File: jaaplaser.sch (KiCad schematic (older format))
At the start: 11 parts

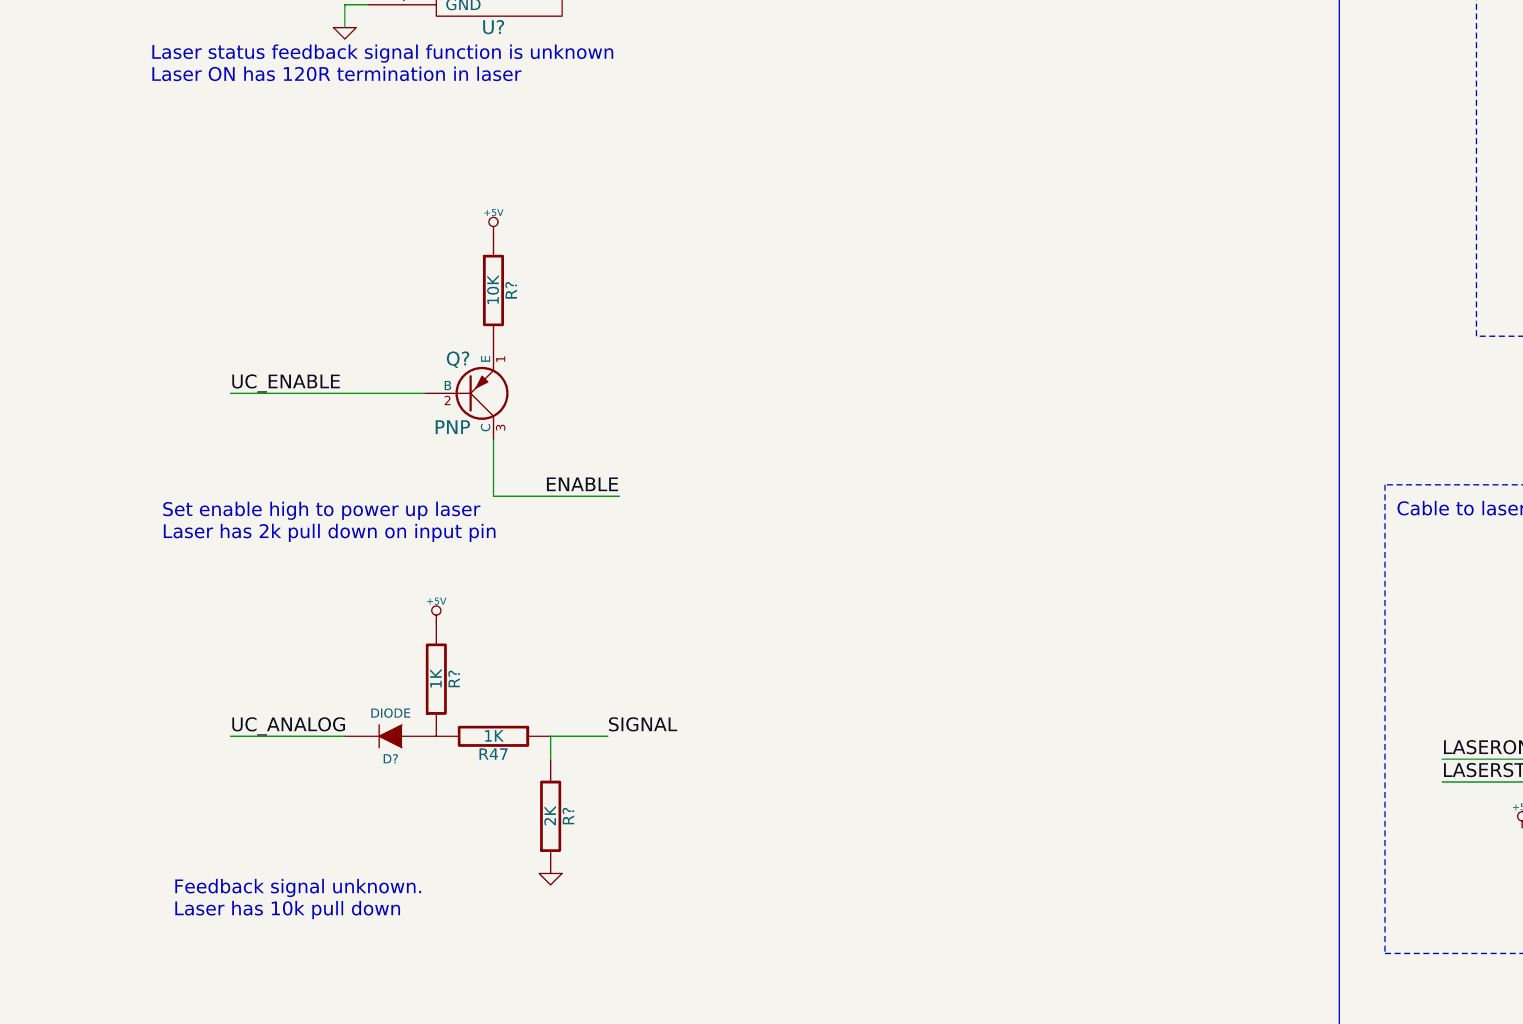
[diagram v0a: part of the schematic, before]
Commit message: added opto-coupler and connections
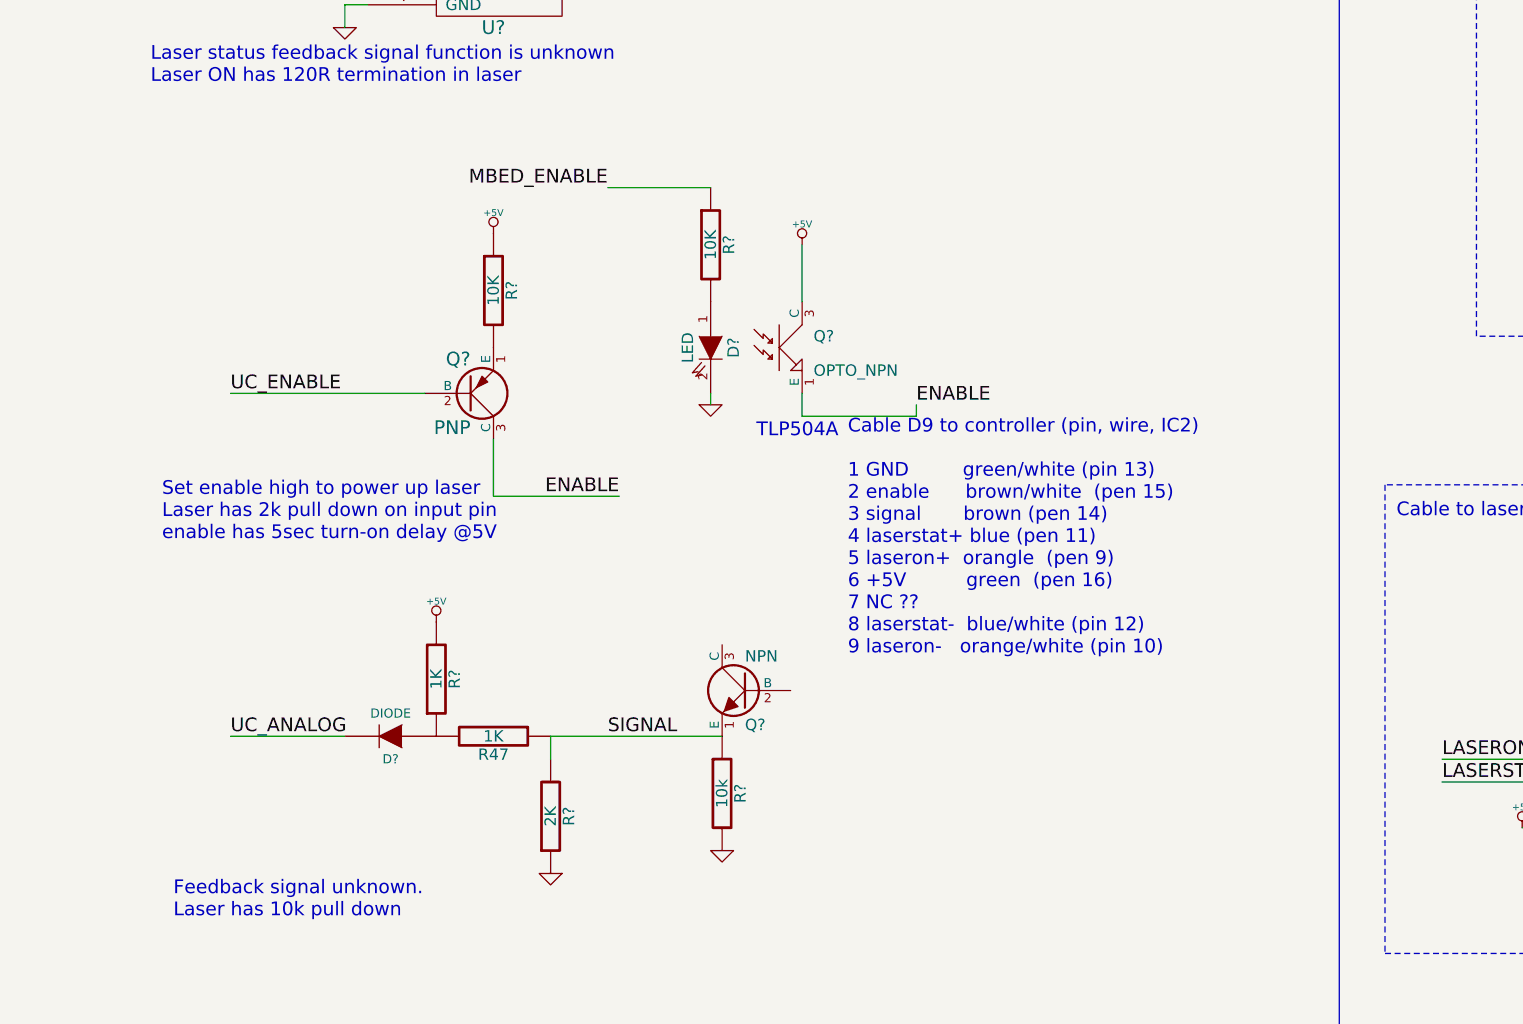
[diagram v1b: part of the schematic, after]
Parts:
- added D?: LED, symbol LED
- added Q?: NPN, symbol NPN
- added Q?: OPTO_NPN, symbol OPTO_NPN
- added R?: 10k, symbol R
- added R?: 10K, symbol R
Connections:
- net +5V: now also Q?.3 (C)
- net ENABLE: now also Q?.1 (E)
- net GND: now also D?.2 (K), R?.2
- net SIGNAL: now also Q?.1 (E), R?.1
- new net: D?.1 (A), R?.2
- new net MBED_ENABLE: R?.1
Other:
- note added: "Cable D9 to controller (pin, wire, IC2)\n\n1 GND green/white (pin 13)\n2 enable brown/white (pen 15)\n3 signal brown (pen 14)\n4 laserstat+ blue (pen 11)\n5 laseron+ orangle (pen 9)\n6 +5V green (pen 16)\n7 NC ?? \n8 laserstat- blue/white (pin 12)\n9 laseron- orange/white (pin 10)\n"
- note added: "Set enable high to power up laser\nLaser has 2k pull down on input pin\nenable has 5sec turn-on delay @5V\n"
- note added: "TLP504A"
- note removed: "Set enable high to power up laser\nLaser has 2k pull down on input pin"
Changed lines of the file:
@@
-EESchema Schematic File Version 2  date 6/1/2014 23:12:49
+EESchema Schematic File Version 2  date 11/22/2015 18:08:19
 LIBS:power
 LIBS:device
@@
 Sheet 1 1
 Title "Lumunics Efx Laser interface"
-Date "1 jun 2014"
+Date "22 nov 2015"
 Rev "1"
 Comp "LaosLaser.org"
@@
 Comment4 ""
 $EndDescr
-Text Notes 7000 4750 0    60   ~ 0
-Cable to laser Header to DB9-Female (flat cable)
+Text Notes 4200 4400 0    60   ~ 0
+TLP504A
+Text Label 3550 3300 2    60   ~ 0
+MBED_ENABLE
+Wire Wire Line
+	4000 3300 3550 3300
+Wire Wire Line
+	4000 4200 4000 4250
+Wire Wire Line
+	4050 5700 3300 5700
 Wire Notes Line
 	11100 4600 11100 6650
@@
 Wire Wire Line
 	3050 4650 3050 4400
-Wire Wire Line
-	3550 5700 3300 5700
 Connection ~ 4500 2300
 Wire Wire Line
@@
 Wire Wire Line
 	9600 5300 9600 5350
+Wire Wire Line
+	4400 3550 4400 3800
+Wire Wire Line
+	4400 4200 4400 4300
+Wire Wire Line
+	4400 4300 4900 4300
+Wire Wire Line
+	4900 4300 4900 4250
+$Comp
+L R R?
+U 1 1 5651F627
+P 4000 3550
+F 0 "R?" V 4080 3550 50  0000 C CNN
+F 1 "10K" V 4000 3550 50  0000 C CNN
+	1    4000 3550
+	1    0    0    -1
+$EndComp
+Text Label 4900 4250 0    60   ~ 0
+ENABLE
+$Comp
+L GND #PWR?
+U 1 1 5651F603
+P 4000 4250
+F 0 "#PWR?" H 4000 4250 30  0001 C CNN
+F 1 "GND" H 4000 4180 30  0001 C CNN
+	1    4000 4250
+	1    0    0    -1
+$EndComp
+$Comp
+L +5V #PWR?
+U 1 1 5651F5F5
+P 4400 3550
+F 0 "#PWR?" H 4400 3640 20  0001 C CNN
+F 1 "+5V" H 4400 3640 30  0000 C CNN
+	1    4400 3550
+	1    0    0    -1
+$EndComp
+$Comp
+L LED D?
+U 1 1 5651F5E6
+P 4000 4000
+F 0 "D?" H 4000 4100 50  0000 C CNN
+F 1 "LED" H 4000 3900 50  0000 C CNN
+	1    4000 4000
+	0    1    1    0
+$EndComp
+$Comp
+L OPTO_NPN Q?
+U 1 1 5651F5D6
+P 4300 4000
+F 0 "Q?" H 4450 4050 50  0000 L CNN
+F 1 "OPTO_NPN" H 4450 3900 50  0000 L CNN
+	1    4300 4000
+	1    0    0    -1
+$EndComp
+$Comp
+L GND #PWR?
+U 1 1 5651CAA0
+P 4050 6200
+F 0 "#PWR?" H 4050 6200 30  0001 C CNN
+F 1 "GND" H 4050 6130 30  0001 C CNN
+	1    4050 6200
+	-1   0    0    -1
+$EndComp
+$Comp
+L R R?
+U 1 1 5651CA94
+P 4050 5950
+F 0 "R?" V 4130 5950 50  0000 C CNN
+F 1 "10k" V 4050 5950 50  0000 C CNN
+	1    4050 5950
+	1    0    0    -1
+$EndComp
+$Comp
+L NPN Q?
+U 1 1 5651CA28
+P 4150 5500
+F 0 "Q?" H 4150 5350 50  0000 R CNN
+F 1 "NPN" H 4150 5650 50  0000 R CNN
+	1    4150 5500
+	-1   0    0    -1
+$EndComp
+Text Notes 4600 5350 0    60   ~ 0
+Cable D9 to controller (pin, wire, IC2)\n\n1 GND         green/white (pin 13)\n2 enable      brown/white  (pen 15)\n3 signal       brown (pen 14)\n4 laserstat+ blue (pen 11)\n5 laseron+  orangle  (pen 9)\n6 +5V          green  (pen 16)\n7 NC ?? \n8 laserstat-  blue/white (pin 12)\n9 laseron-   orange/white (pin 10)\n
+Text Notes 7000 4750 0    60   ~ 0
+Cable to laser Header to DB9-Female (flat cable)
 $Comp
 L GND #PWR?
@@
 Feedback signal unknown. \nLaser has 10k pull down
 Text Notes 1600 4850 0    60   ~ 0
-Set enable high to power up laser\nLaser has 2k pull down on input pin
+Set enable high to power up laser\nLaser has 2k pull down on input pin\nenable has 5sec turn-on delay @5V\n
 Text Notes 1550 2850 0    60   ~ 0
 Laser status feedback signal function is unknown\nLaser ON has 120R termination in laser
